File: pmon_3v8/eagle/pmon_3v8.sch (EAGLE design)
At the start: 39 parts, among them J1 USB, J2 USB, J4 PINHD-1X3, J5 PINHD-2X3, Q1 16Mhz, U1 LTC2943, U2 FT232RL, U3 LT1764AEQ, U4 ATMEGA328TQFP32, U5 TC1015

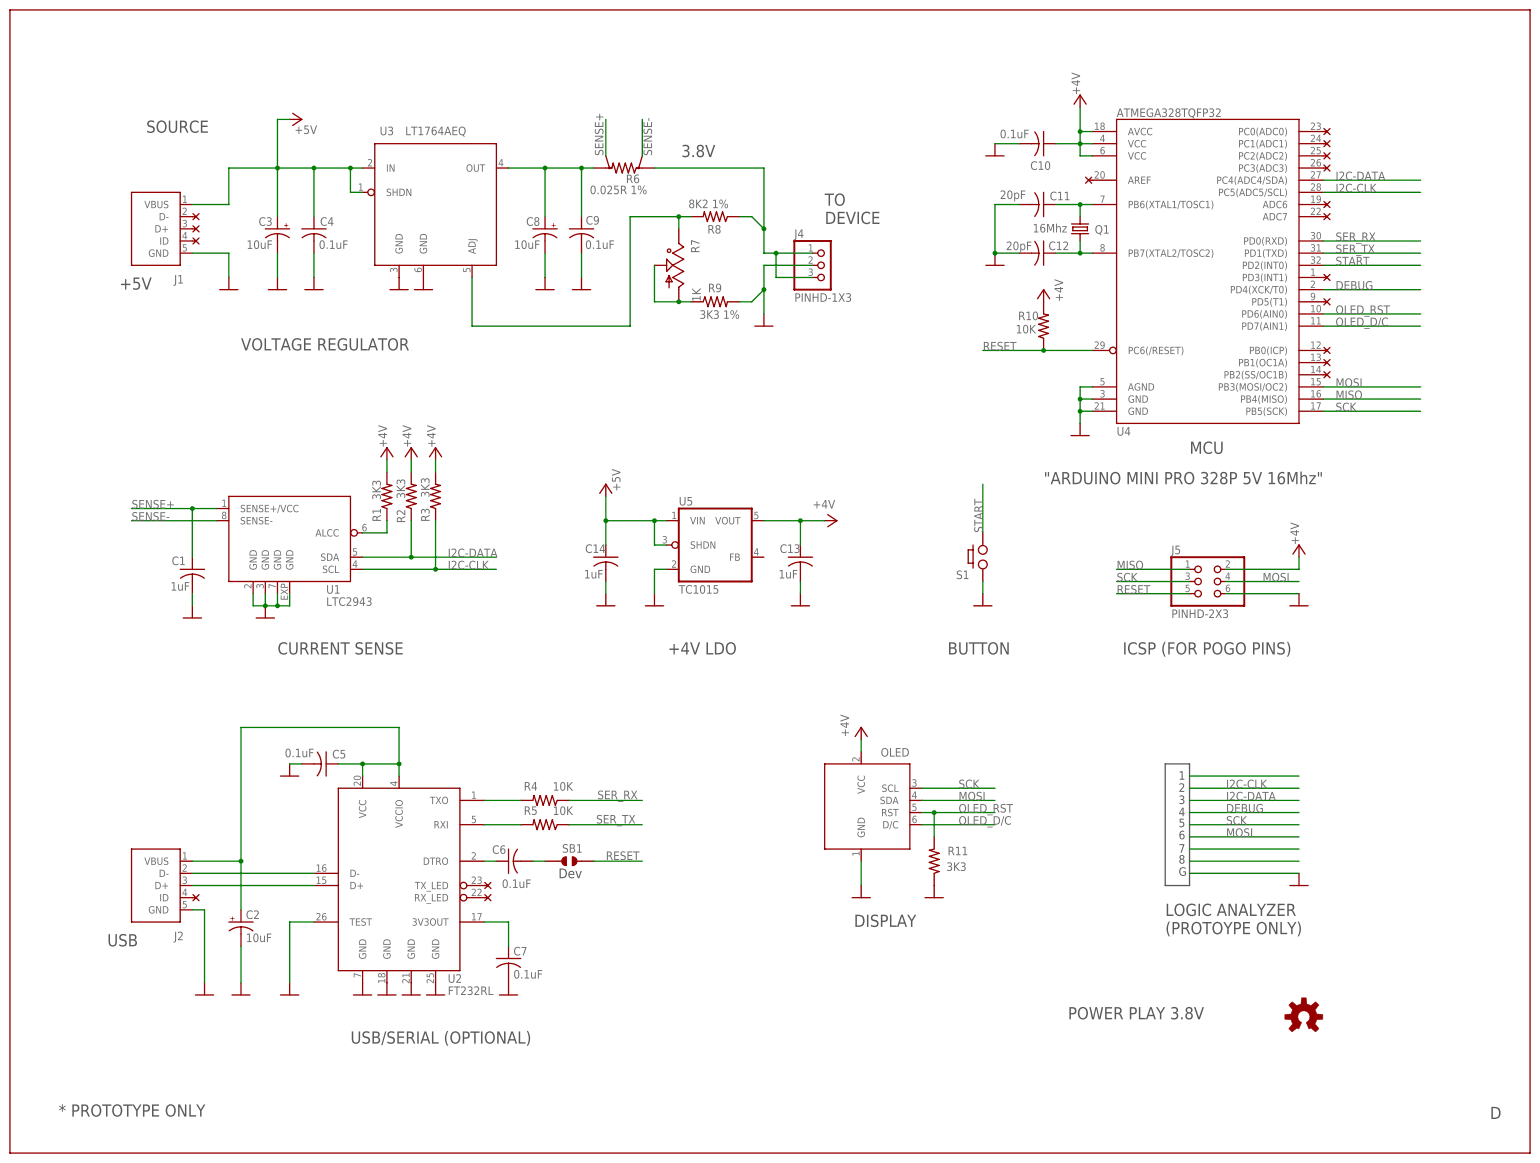
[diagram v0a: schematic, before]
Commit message: Renamed +4V network to VCC. No semantic change.
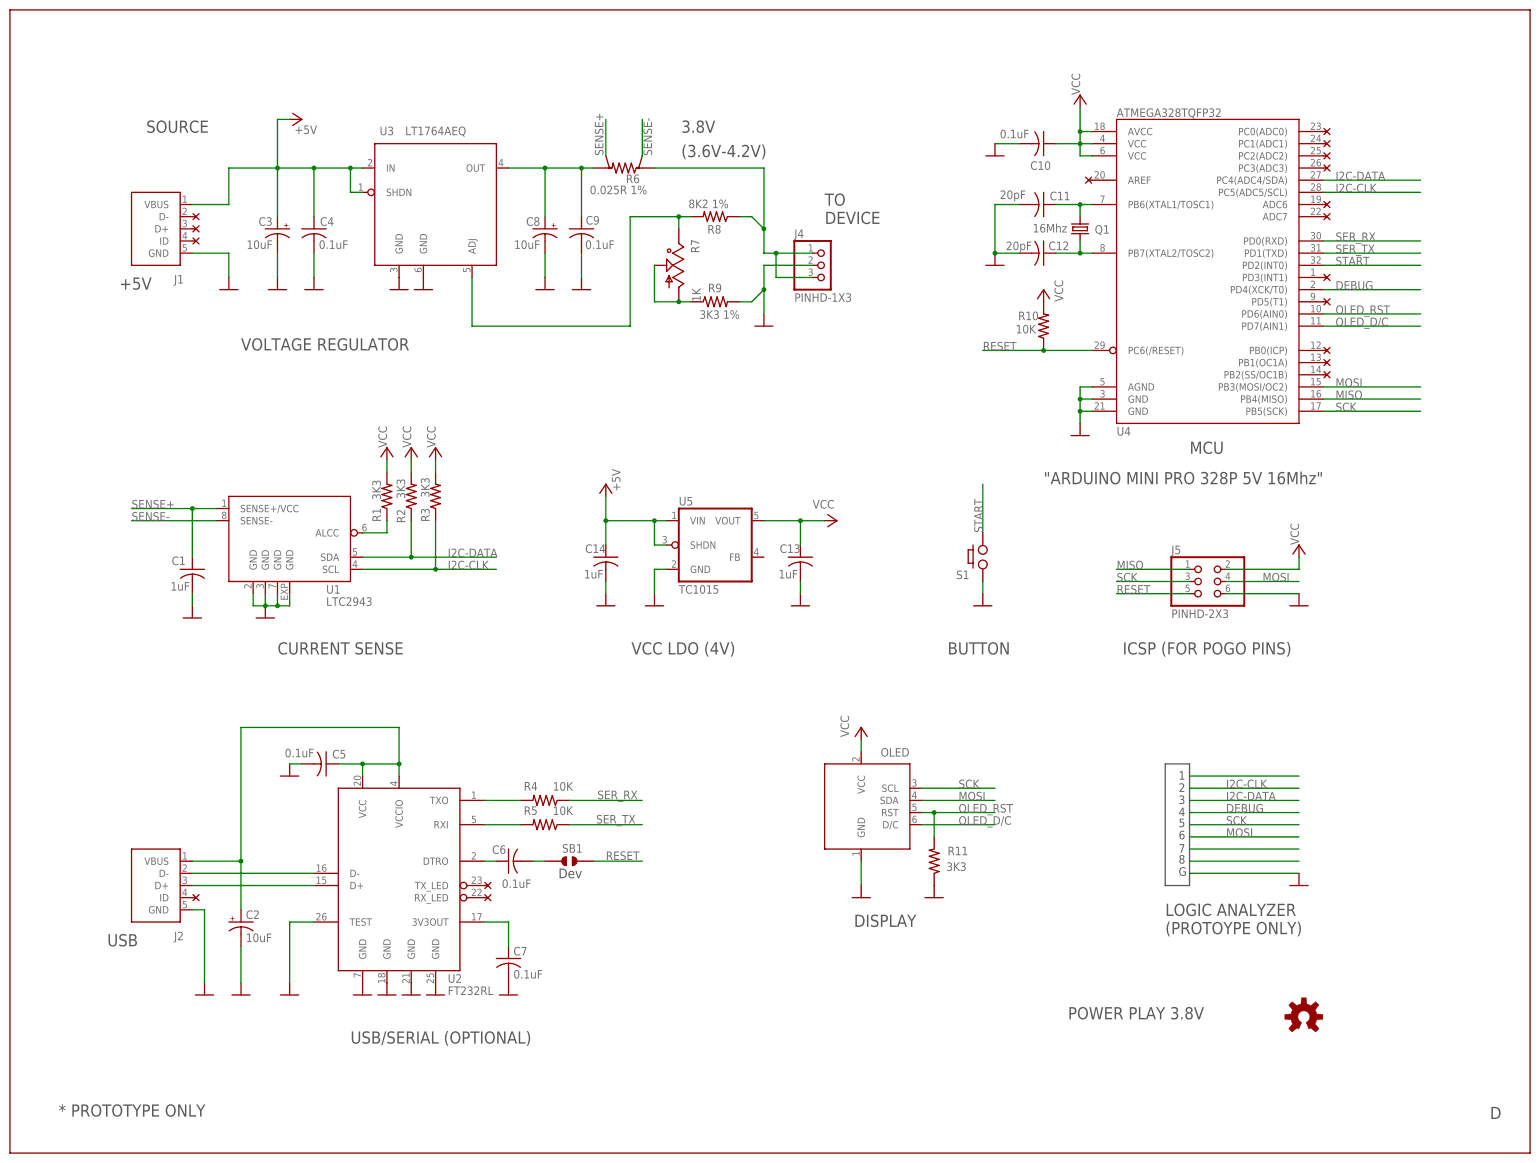
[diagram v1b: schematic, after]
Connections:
- net +4V renamed VCC
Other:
- note added: "(3.6V-4.2V)"
- note added: "VCC LDO (4V)"
- note removed: "+4V LDO"
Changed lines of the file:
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@@
 <part name="GND2" library="pmon_3v8" deviceset="GND" device=""/>
 <part name="U5" library="pmon_3v8" deviceset="TC1015" device=""/>
-<part name="U$1" library="pmon_3v8" deviceset="+4V" device=""/>
-<part name="U$21" library="pmon_3v8" deviceset="+4V" device=""/>
-<part name="U$22" library="pmon_3v8" deviceset="+4V" device=""/>
-<part name="U$23" library="pmon_3v8" deviceset="+4V" device=""/>
-<part name="U$24" library="pmon_3v8" deviceset="+4V" device=""/>
-<part name="U$25" library="pmon_3v8" deviceset="+4V" device=""/>
-<part name="U$26" library="pmon_3v8" deviceset="+4V" device=""/>
-<part name="U$27" library="pmon_3v8" deviceset="+4V" device=""/>
+<part name="U$1" library="pmon_3v8" deviceset="VCC" device=""/>
+<part name="U$21" library="pmon_3v8" deviceset="VCC" device=""/>
+<part name="U$22" library="pmon_3v8" deviceset="VCC" device=""/>
+<part name="U$23" library="pmon_3v8" deviceset="VCC" device=""/>
+<part name="U$24" library="pmon_3v8" deviceset="VCC" device=""/>
+<part name="U$25" library="pmon_3v8" deviceset="VCC" device=""/>
+<part name="U$26" library="pmon_3v8" deviceset="VCC" device=""/>
+<part name="U$27" library="pmon_3v8" deviceset="VCC" device=""/>
 <part name="P+1" library="pmon_3v8" deviceset="+5V" device=""/>
 <part name="GND3" library="pmon_3v8" deviceset="GND" device=""/>
@@
 <text x="134.62" y="194.056" size="2.54" layer="97">TO
 DEVICE</text>
-<text x="104.648" y="208.026" size="2.54" layer="97">3.8V</text>
+<text x="104.648" y="213.106" size="2.54" layer="97">3.8V</text>
 <text x="208.534" y="77.978" size="1.778" layer="97">1</text>
 <text x="208.534" y="75.438" size="1.778" layer="97">2</text>
@@
 <text x="78.994" y="57.404" size="2.032" layer="97">Dev</text>
 <text x="273.558" y="7.112" size="2.54" layer="97">D</text>
-<text x="101.854" y="104.14" size="2.54" layer="97">+4V LDO</text>
+<text x="94.234" y="104.14" size="2.54" layer="97">VCC LDO (4V)</text>
+<text x="104.648" y="208.026" size="2.54" layer="97">(3.6V-4.2V)</text>
 </plain>
 <instances>
@@
 </segment>
 </net>
-<net name="+4V" class="0">
+<net name="VCC" class="0">
 <segment>
 <pinref part="U5" gate="G$1" pin="VOUT"/>
 <wire x1="121.92" y1="132.08" x2="129.54" y2="132.08" width="0.1524" layer="91"/>
-<pinref part="U$1" gate="G$1" pin="+4V"/>
+<pinref part="U$1" gate="G$1" pin="VCC"/>
 <pinref part="C13" gate="G$1" pin="1"/>
 <wire x1="129.54" y1="132.08" x2="134.62" y2="132.08" width="0.1524" layer="91"/>
@@
 <pinref part="R1" gate="G$1" pin="2"/>
 <wire x1="43.18" y1="144.78" x2="43.18" y2="142.24" width="0.1524" layer="91"/>
-<pinref part="U$21" gate="G$1" pin="+4V"/>
+<pinref part="U$21" gate="G$1" pin="VCC"/>
 </segment>
 <segment>
 <pinref part="R2" gate="G$1" pin="2"/>
 <wire x1="48.26" y1="144.78" x2="48.26" y2="142.24" width="0.1524" layer="91"/>
-<pinref part="U$22" gate="G$1" pin="+4V"/>
+<pinref part="U$22" gate="G$1" pin="VCC"/>
 </segment>
 <segment>
 <pinref part="R3" gate="G$1" pin="2"/>
 <wire x1="53.34" y1="144.78" x2="53.34" y2="142.24" width="0.1524" layer="91"/>
-<pinref part="U$23" gate="G$1" pin="+4V"/>
+<pinref part="U$23" gate="G$1" pin="VCC"/>
 </segment>
 <segment>
@@
 <pinref part="U4" gate="G$1" pin="VCC@1"/>
 <pinref part="U4" gate="G$1" pin="VCC@2"/>
-<pinref part="U$24" gate="G$1" pin="+4V"/>
+<pinref part="U$24" gate="G$1" pin="VCC"/>
 </segment>
 <segment>
@@
 <wire x1="218.44" y1="121.92" x2="233.68" y2="121.92" width="0.1524" layer="91"/>
 <wire x1="233.68" y1="121.92" x2="233.68" y2="124.46" width="0.1524" layer="91"/>
-<pinref part="U$25" gate="G$1" pin="+4V"/>
+<pinref part="U$25" gate="G$1" pin="VCC"/>
 </segment>
 <segment>
 <pinref part="R10" gate="G$1" pin="2"/>
-<pinref part="U$26" gate="G$1" pin="+4V"/>
+<pinref part="U$26" gate="G$1" pin="VCC"/>
 </segment>
 <segment>
 <pinref part="OLED" gate="G$1" pin="VCC"/>
 <wire x1="142.24" y1="83.82" x2="142.24" y2="86.36" width="0.1524" layer="91"/>
-<pinref part="U$27" gate="G$1" pin="+4V"/>
-</segment>
-</net>
+<pinref part="U$27" gate="G$1" pin="VCC"/>
+</segment>
+</net>
